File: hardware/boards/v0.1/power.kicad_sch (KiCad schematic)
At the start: 63 parts, among them IC3 SP3401-02UTG, J2 USB, U20 TPS62A02DRL, U23 BQ21040DBV, U30 FUSB307BMPX, U31 TPS22929D, U32 LTC2942, U36 STM6601CQ2DDM6x, U39 TPS61252DSG, U40 MIC2017YM6

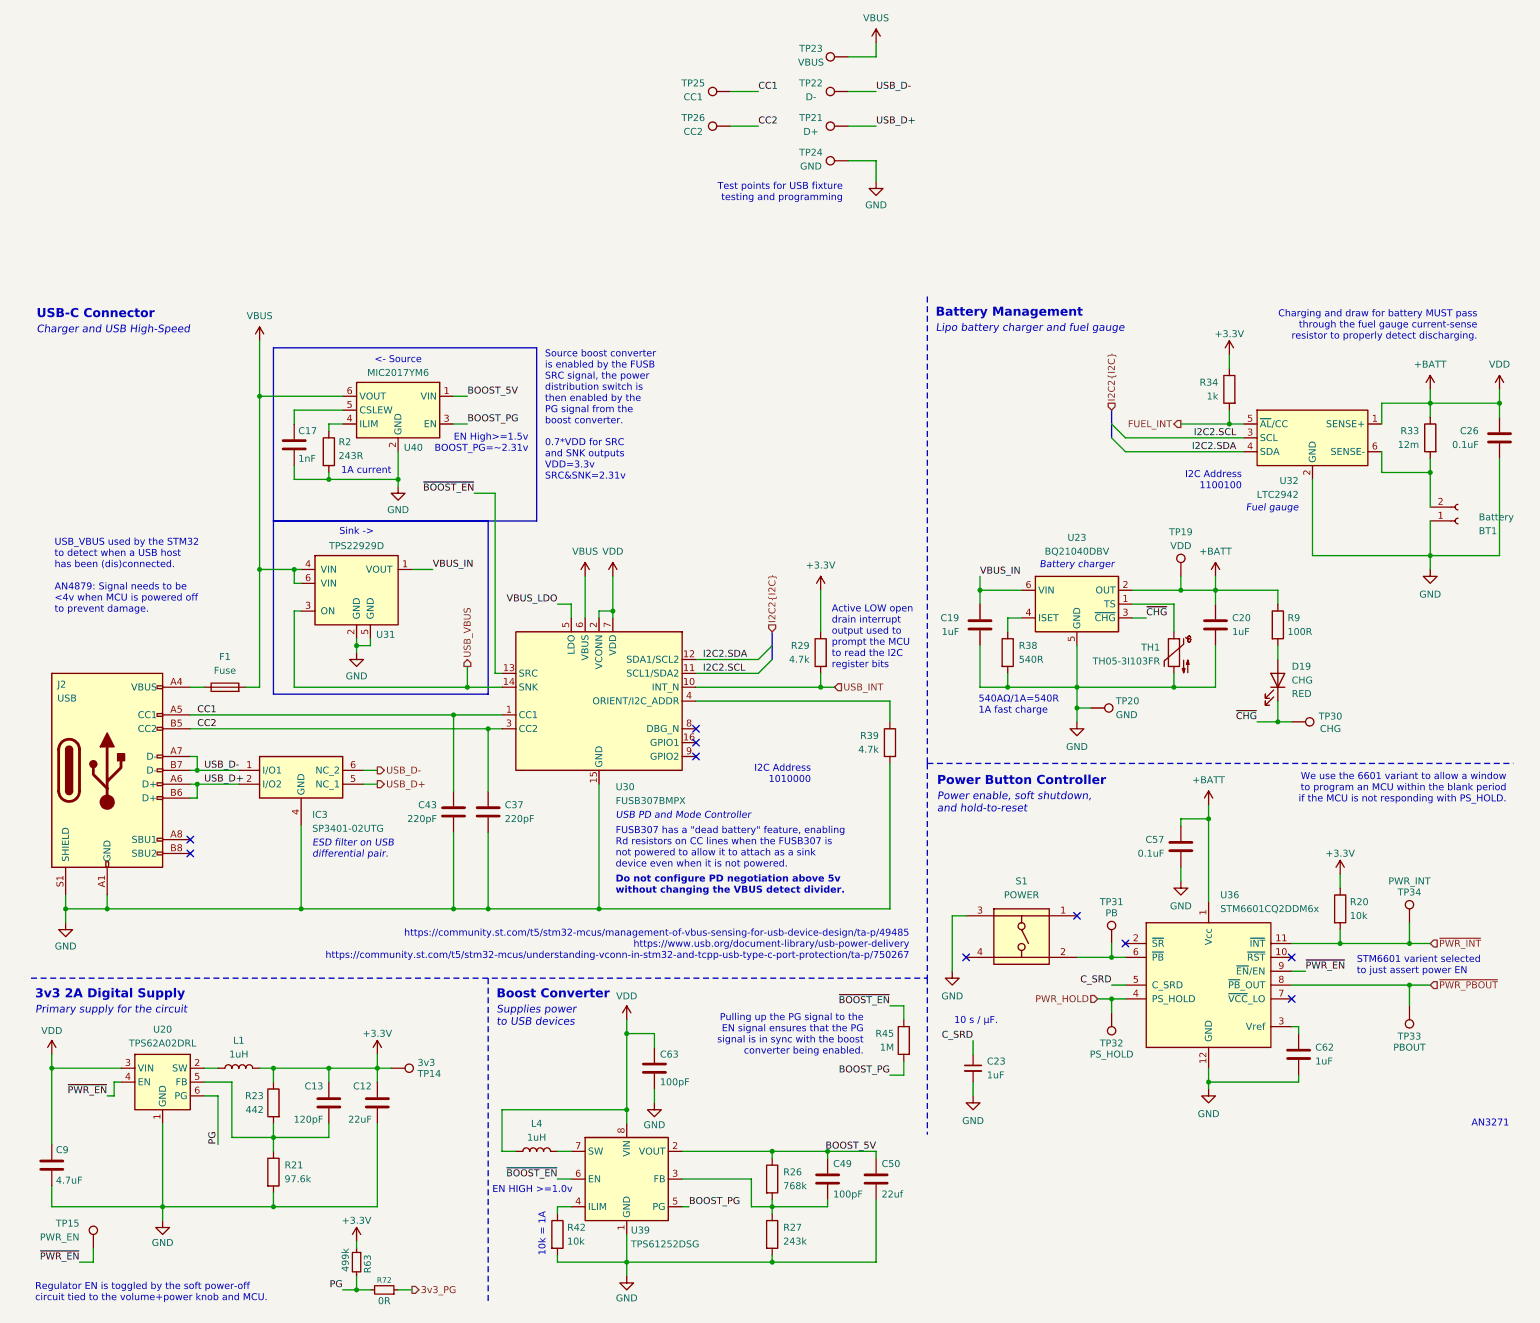
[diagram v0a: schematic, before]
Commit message: feat: routing cleanup and start of BOM selection
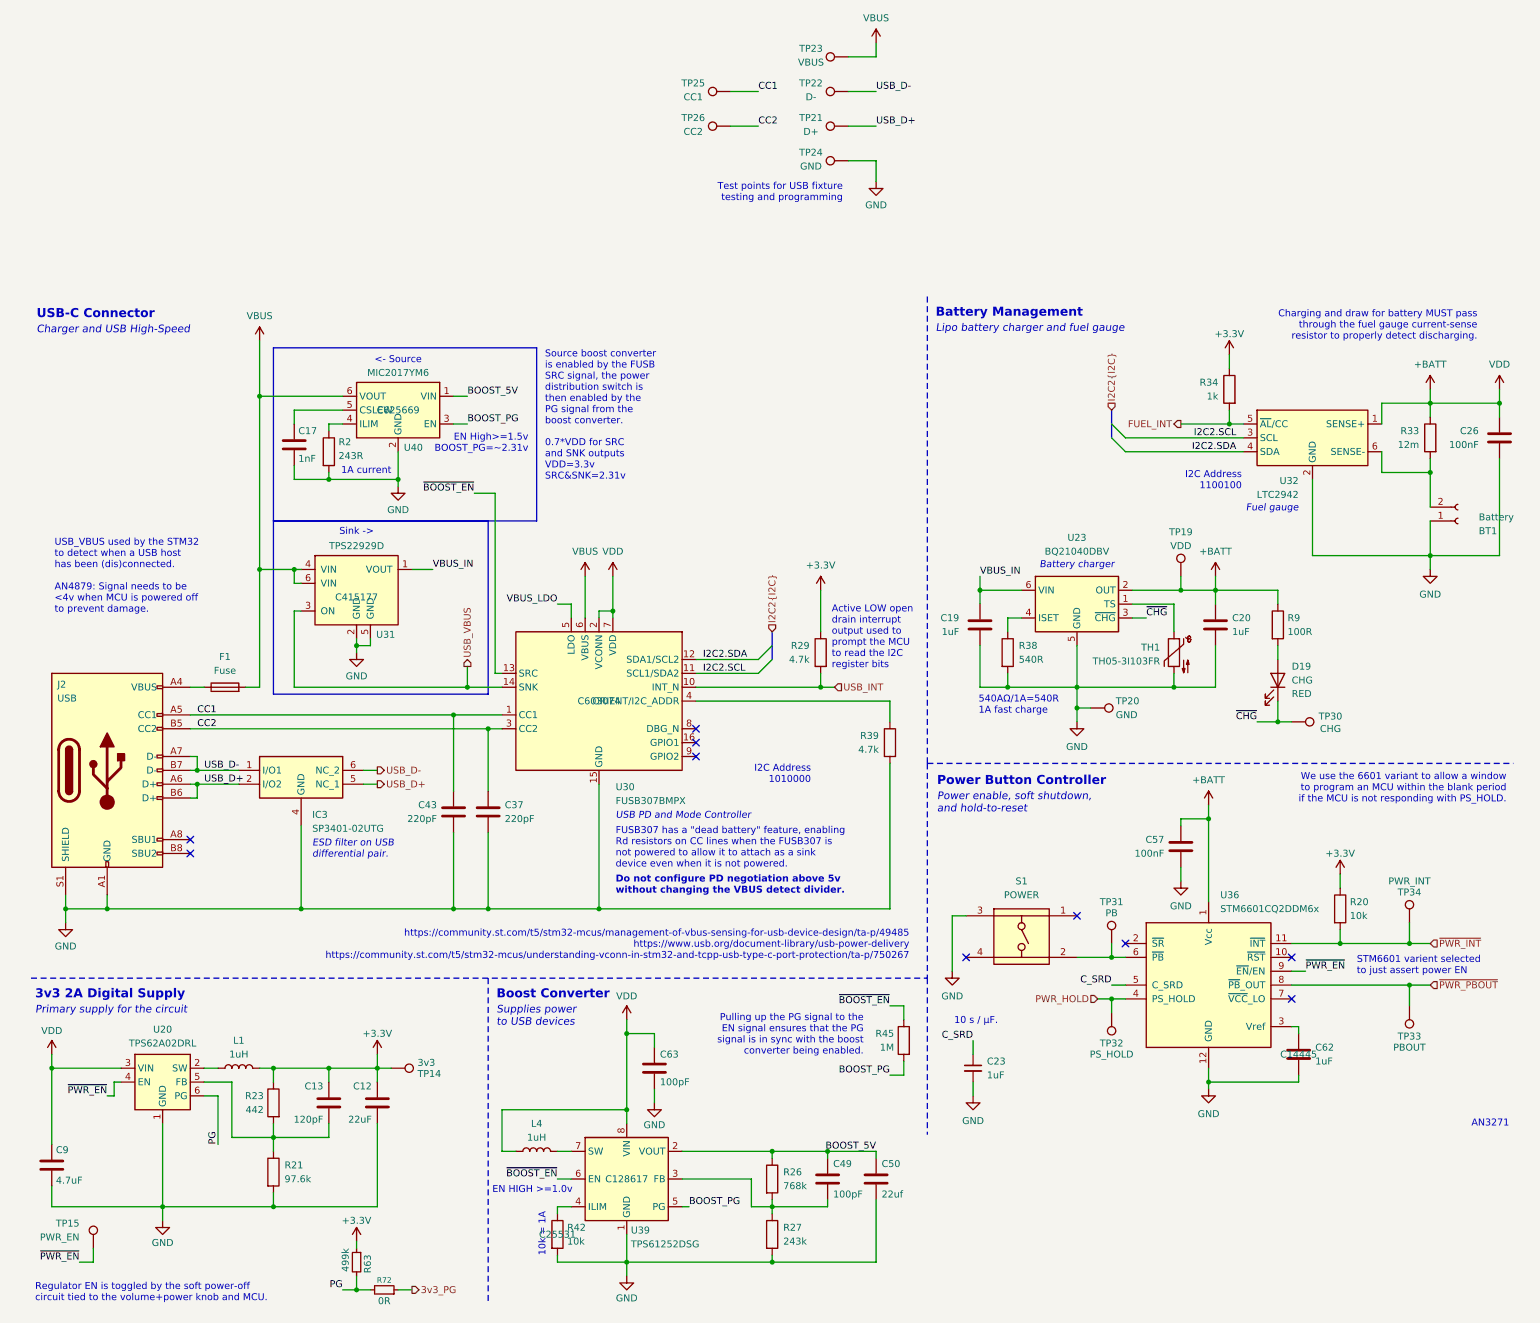
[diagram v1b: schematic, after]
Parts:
- BT1: JLC (none) -> C295747
- C12: footprint Capacitor_SMD:C_0603_1608Metric -> Capacitor_SMD:C_0402_1005Metric; JLC (none) -> C415703
- C13: footprint Capacitor_SMD:C_0603_1608Metric -> Capacitor_SMD:C_0402_1005Metric; JLC (none) -> C40059
- C23, C62: JLC (none) -> C14445
- C26: value 0.1uF -> 100nF; footprint Capacitor_SMD:C_0603_1608Metric -> Capacitor_SMD:C_0402_1005Metric; JLC (none) -> C1525
- C37, C43: JLC (none) -> C1530
- C49: JLC (none) -> C1546
- C50: JLC (none) -> C415703
- C57: value 0.1uF -> 100nF; JLC (none) -> C1525
- R2: JLC (none) -> C25095
- R20, R42: JLC (none) -> C25531
- R26: JLC (none) -> C27017
- R27: JLC (none) -> C43249
- R39: JLC (none) -> C25900
- R45: JLC (none) -> C26083
- TH1: JLC (none) -> C3154728
- TP14, TP15, TP19, TP20, TP21, TP22, TP23, TP24, TP25, TP26, TP30, TP31, TP32, TP33, TP34: now left out of the parts list
- U30: JLC (none) -> C603074
- U31: JLC (none) -> C415177
- U39: JLC (none) -> C128617
- U40: JLC (none) -> C625669

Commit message: feat: update various components to 0402
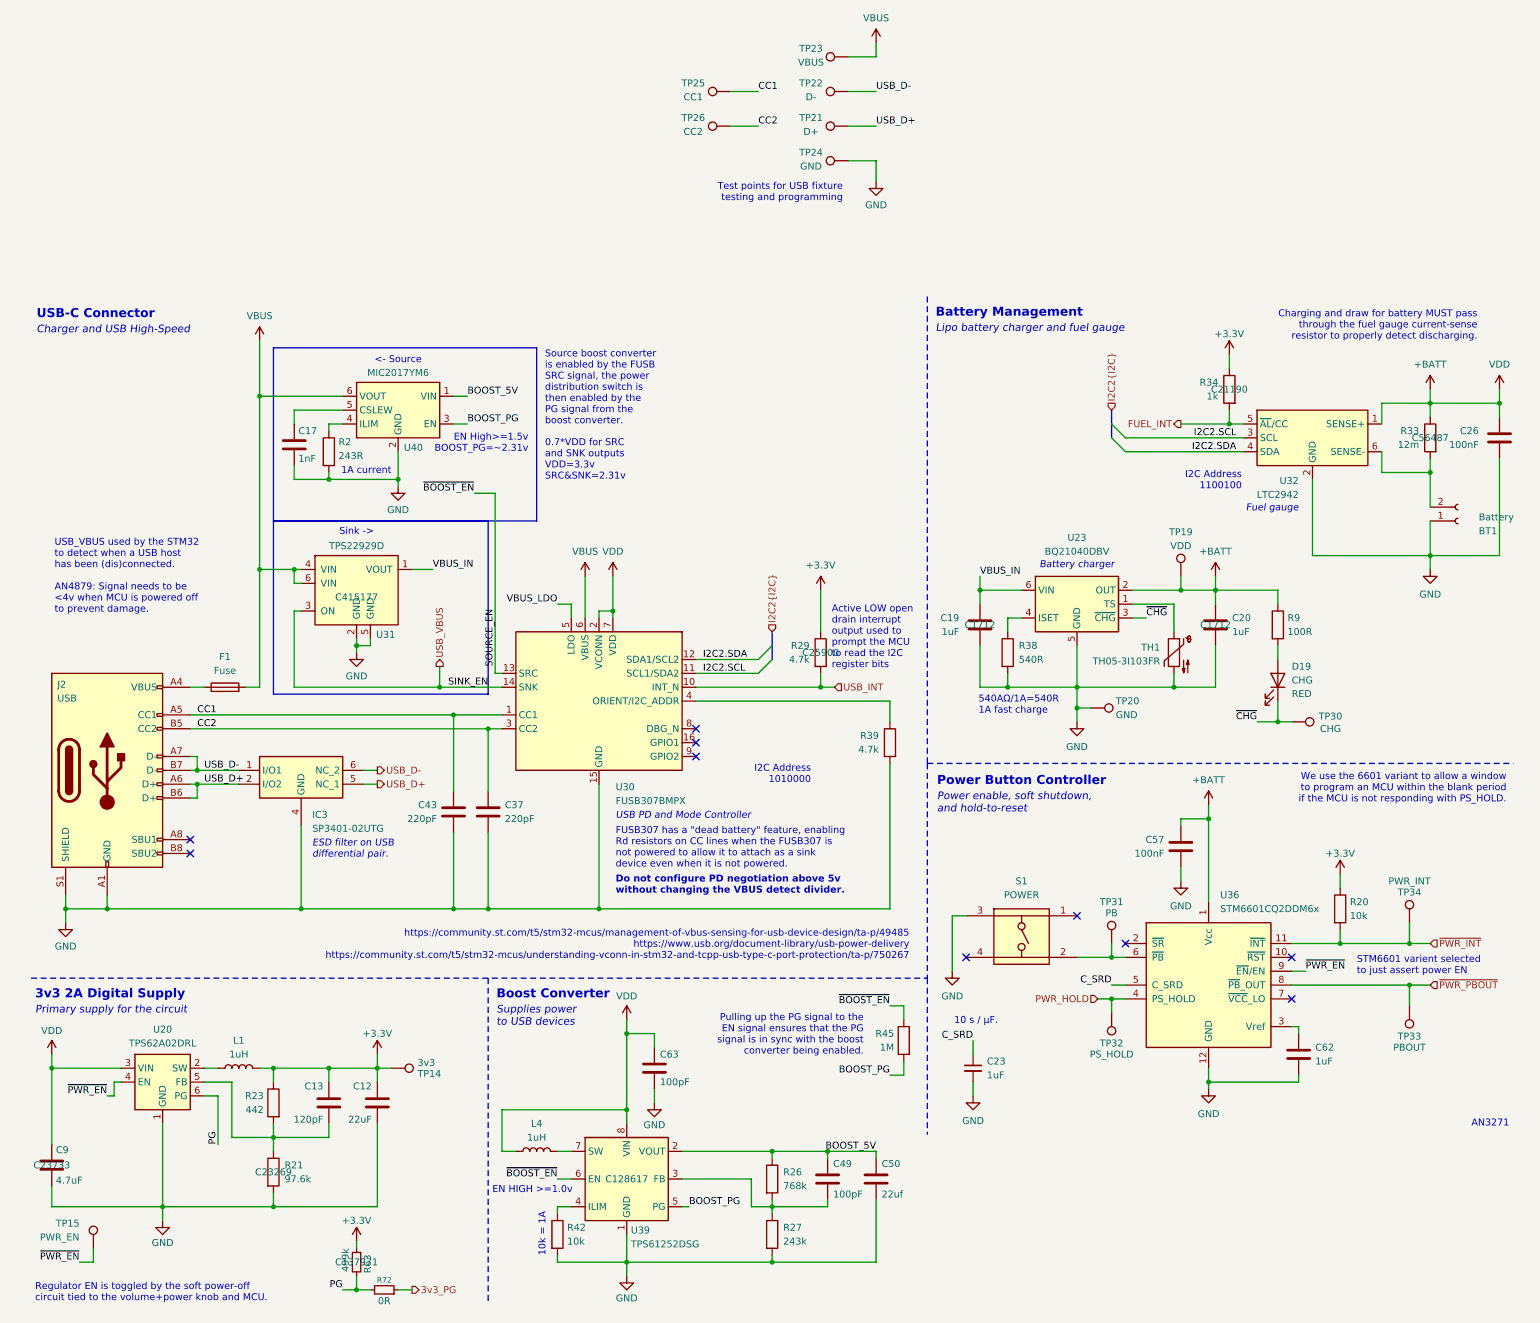
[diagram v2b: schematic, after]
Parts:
- C17: footprint (none) -> Capacitor_SMD:C_0402_1005Metric; JLC (none) -> C1523
- C19, C20: JLC (none) -> C1712
- C63: footprint Capacitor_SMD:C_0603_1608Metric -> Capacitor_SMD:C_0402_1005Metric; JLC (none) -> C1546
- C9: footprint Capacitor_SMD:C_0603_1608Metric -> Capacitor_SMD:C_0402_1005Metric; JLC (none) -> C23733
- IC3: Mouser Part Number 576-SP3401-02UTG -> (none); Mouser Price/Stock https://www.mouser.co.uk/ProductDetail/Littelfuse/SP3401-02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 -> (none)
- R21: JLC (none) -> C23269
- R29: footprint Resistor_SMD:R_0603_1608Metric -> Resistor_SMD:R_0402_1005Metric; JLC (none) -> C25900
- R33: footprint Resistor_SMD:R_2512_6332Metric_Pad1.40x3.35mm_HandSolder -> Resistor_SMD:R_1206_3216Metric_Pad1.30x1.75mm_HandSolder; JLC (none) -> C56487
- R34: JLC (none) -> C21190
- R63: footprint Resistor_SMD:R_0603_1608Metric -> Resistor_SMD:R_0402_1005Metric; JLC (none) -> C137971
- S1: Mouser Part Number 710-436331045822 -> (none); Mouser Price/Stock https://www.mouser.co.uk/ProductDetail/Wurth-Elektronik/436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 -> (none)
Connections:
- net ~{BOOST_EN} renamed SOURCE_EN

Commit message: feat: various DFM cleanup steps
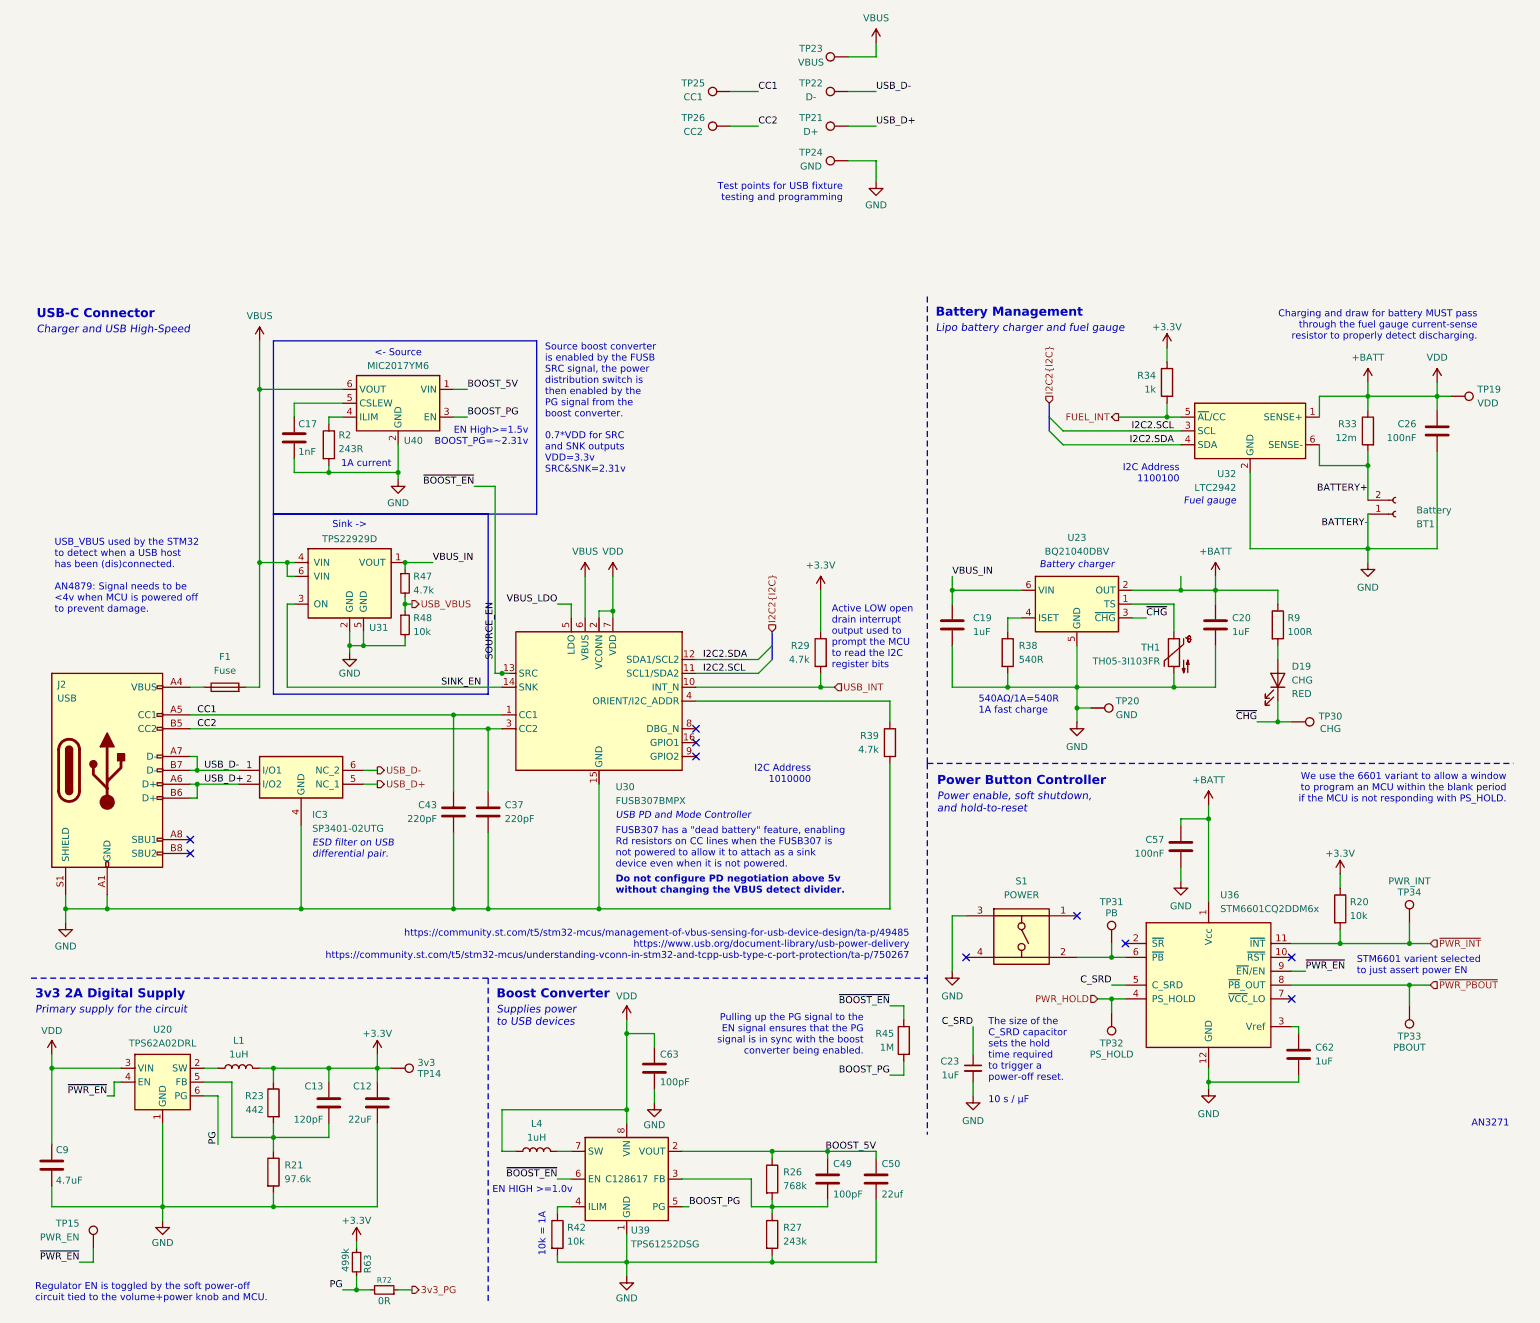
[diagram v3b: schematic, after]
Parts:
- added R47: 4.7k, Resistor_SMD:R_0402_1005Metric, symbol Device:R_Small
- added R48: 10k, Resistor_SMD:R_0402_1005Metric, symbol Device:R_Small
- C12: footprint Capacitor_SMD:C_0402_1005Metric -> Capacitor_SMD:C_0805_2012Metric; JLC C415703 -> (none)
- C13: footprint Capacitor_SMD:C_0402_1005Metric -> Capacitor_SMD:C_0805_2012Metric; JLC C40059 -> (none)
- C26: footprint Capacitor_SMD:C_0402_1005Metric -> Capacitor_SMD:C_0603_1608Metric; JLC C1525 -> (none)
- D19: footprint LED_SMD:LED_0805_2012Metric_Pad1.15x1.40mm_HandSolder -> LED_SMD:LED_0402_1005Metric
- R9: footprint Resistor_SMD:R_0603_1608Metric -> Resistor_SMD:R_0402_1005Metric
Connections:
- net GND: now also R48.2
- net USB_VBUS: now also R47.2, R48.1; no longer U30.14 (SNK), U31.3 (ON)
- net VBUS_IN: now also R47.1
- net BATTERY+: now reaches BT1.2 (Pin_2), R33.2, U32.6 (SENSE-)
- new net SINK_EN: U30.14 (SNK), U31.3 (ON)
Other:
- note added: "The size of the C_SRD capacitor sets the hold time required to trigger a power-off reset. 10 s / µF"
- note removed: "10 s / µF."
- moved on the sheet: BT1, C17, C19, C26, R2, R33, R34, TP19, U31, U32, U40
